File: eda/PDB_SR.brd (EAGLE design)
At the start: 101.6 x 81.3 mm, 18 parts

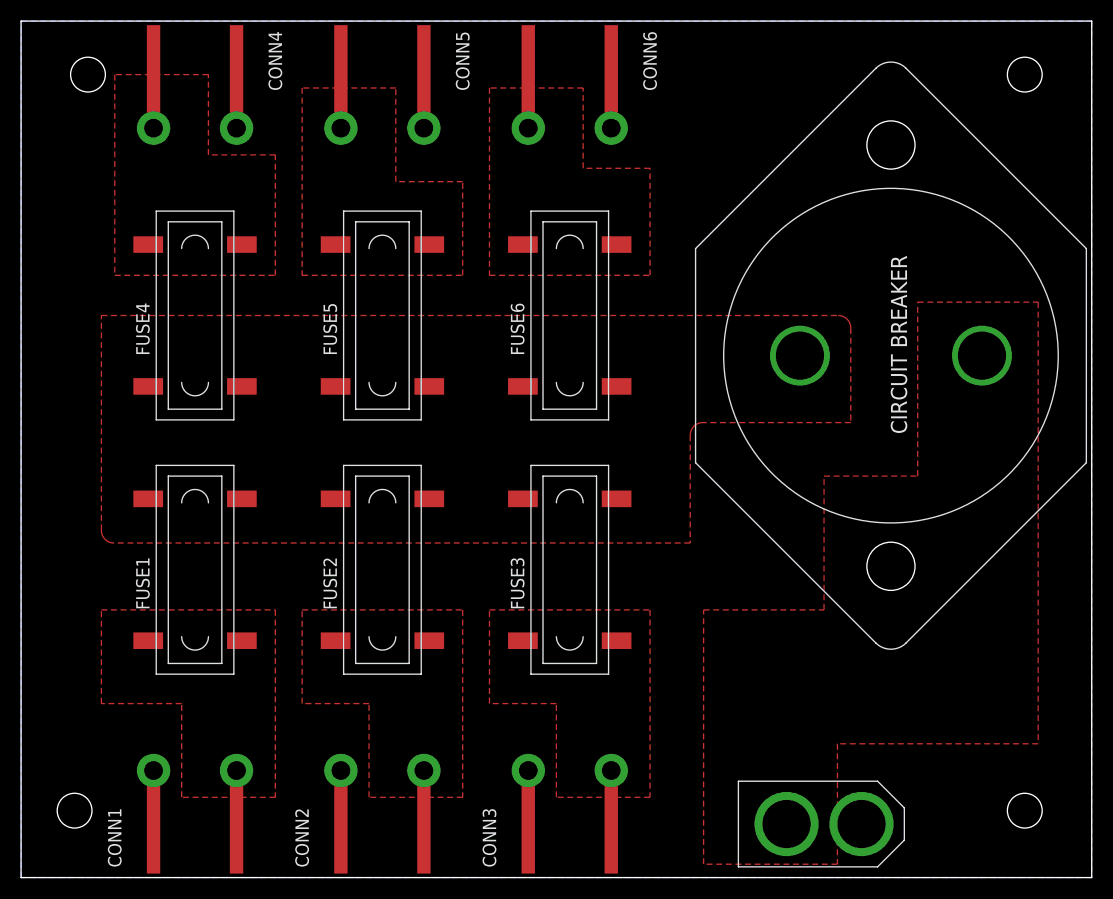
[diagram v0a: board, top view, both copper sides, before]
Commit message: Revert "Updated PDB Design"
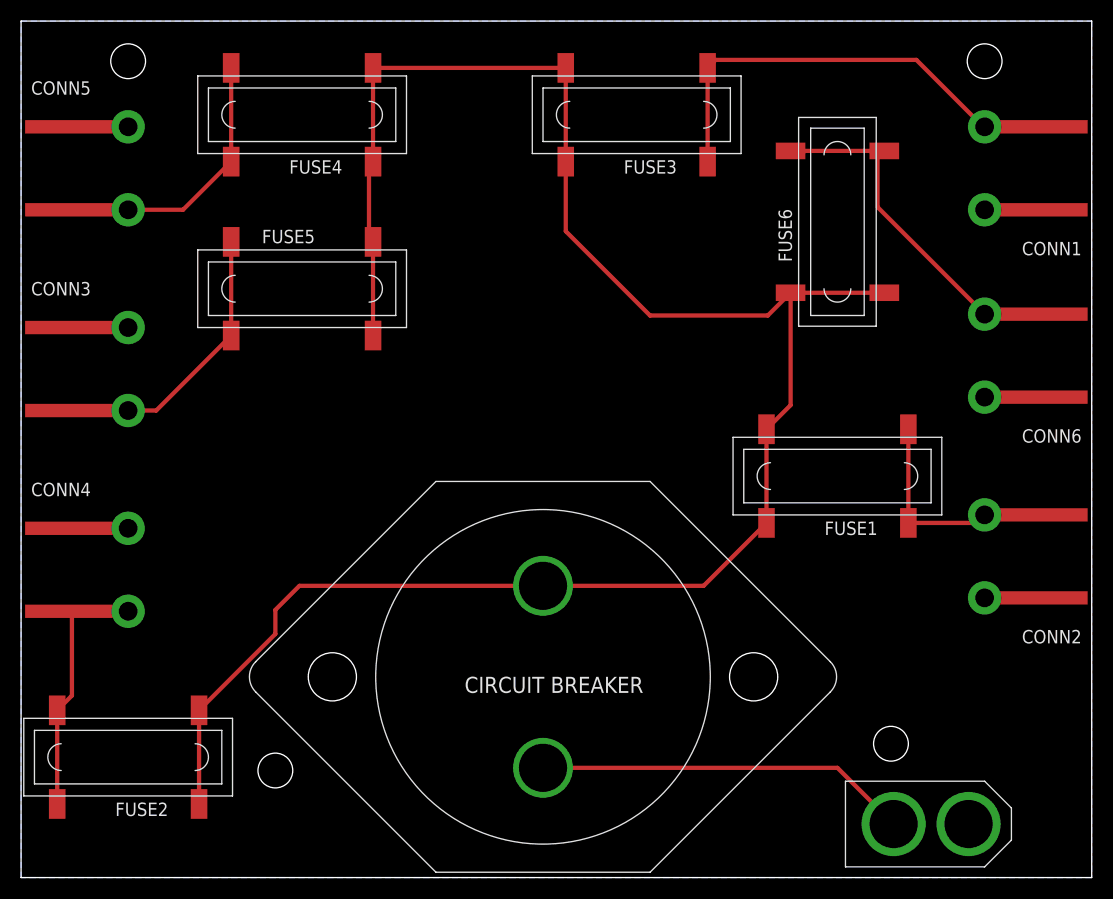
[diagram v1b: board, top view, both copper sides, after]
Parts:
- moved CONN1 94.2 mm to (91.4, 67.3), turned to 180 degrees
- moved FUSE1 61.6 mm to (77.5, 38.1), turned to 180 degrees
- moved CONN2 60.7 mm to (91.4, 30.5), turned to 180 degrees
- moved CONN3 56.6 mm to (10.2, 48.3), turned to 0 degrees
- moved CIRCUIT_BREAKER 44.9 mm to (49.5, 19.1), turned to 180 degrees
- moved CONN6 44.9 mm to (91.4, 49.5), turned to 180 degrees
- moved FUSE3 43.6 mm to (58.4, 72.4), turned to 180 degrees
- moved CONN4 42.4 mm to (10.2, 29.2), turned to 0 degrees
- moved FUSE2 30.0 mm to (10.2, 11.4), turned to 180 degrees
- moved FUSE6 26.9 mm to (77.5, 62.2)
- moved CONN5 24.4 mm to (10.2, 67.3), turned to 0 degrees
- moved FUSE4 21.6 mm to (26.7, 72.4), turned to 180 degrees
- moved U$2 19.4 mm to (24.1, 10.2)
- moved U$5 14.2 mm to (82.5, 12.7)
- moved U$1 10.2 mm to (86.4, 5.08)
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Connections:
- net 12V: now also FUSE2.P$1_DOWN, FUSE2.P$1_UP, FUSE5.P$2_DOWN, FUSE5.P$2_UP; no longer FUSE2.P$2_DOWN, FUSE2.P$2_UP, FUSE5.P$1_DOWN, FUSE5.P$1_UP
- net VOUT1: now also CONN2.PIN2, CONN2.PIN2-LEAD; no longer CONN1.PIN2, CONN1.PIN2-LEAD
- net VOUT2: now also CONN4.PIN2, CONN4.PIN2-LEAD, FUSE2.P$2_DOWN, FUSE2.P$2_UP; no longer CONN2.PIN2, CONN2.PIN2-LEAD, FUSE2.P$1_DOWN, FUSE2.P$1_UP
- net VOUT3: now also CONN1.PIN2, CONN1.PIN2-LEAD; no longer CONN3.PIN2, CONN3.PIN2-LEAD
- net VOUT4: now also CONN5.PIN2, CONN5.PIN2-LEAD; no longer CONN4.PIN2, CONN4.PIN2-LEAD
- net VOUT5: now also CONN3.PIN2, CONN3.PIN2-LEAD, FUSE5.P$1_DOWN, FUSE5.P$1_UP; no longer CONN5.PIN2, CONN5.PIN2-LEAD, FUSE5.P$2_DOWN, FUSE5.P$2_UP
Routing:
- net 12V: track 0.00 -> 189.9 mm
- net VOUT3: track 5.33 -> 43.6 mm
- net BAT: track 0.00 -> 35.5 mm
- net VOUT6: track 5.33 -> 34.3 mm
- net VOUT4: track 5.33 -> 28.7 mm
- net VOUT5: track 5.33 -> 26.9 mm
- net VOUT2: track 5.33 -> 24.2 mm
- net VOUT1: track 5.33 -> 21.8 mm
- removed copper zone on layer 1, net 12V
- removed copper zone on layer 1, net BAT
- removed copper zone on layer 1, net VOUT1
- removed copper zone on layer 1, net VOUT2
- removed copper zone on layer 1, net VOUT3
- removed copper zone on layer 1, net VOUT4
- removed copper zone on layer 1, net VOUT5
- removed copper zone on layer 1, net VOUT6
